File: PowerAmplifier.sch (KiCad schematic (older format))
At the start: 36 parts, among them K1 INPUT, K3 OUTPUT, P1 POWER

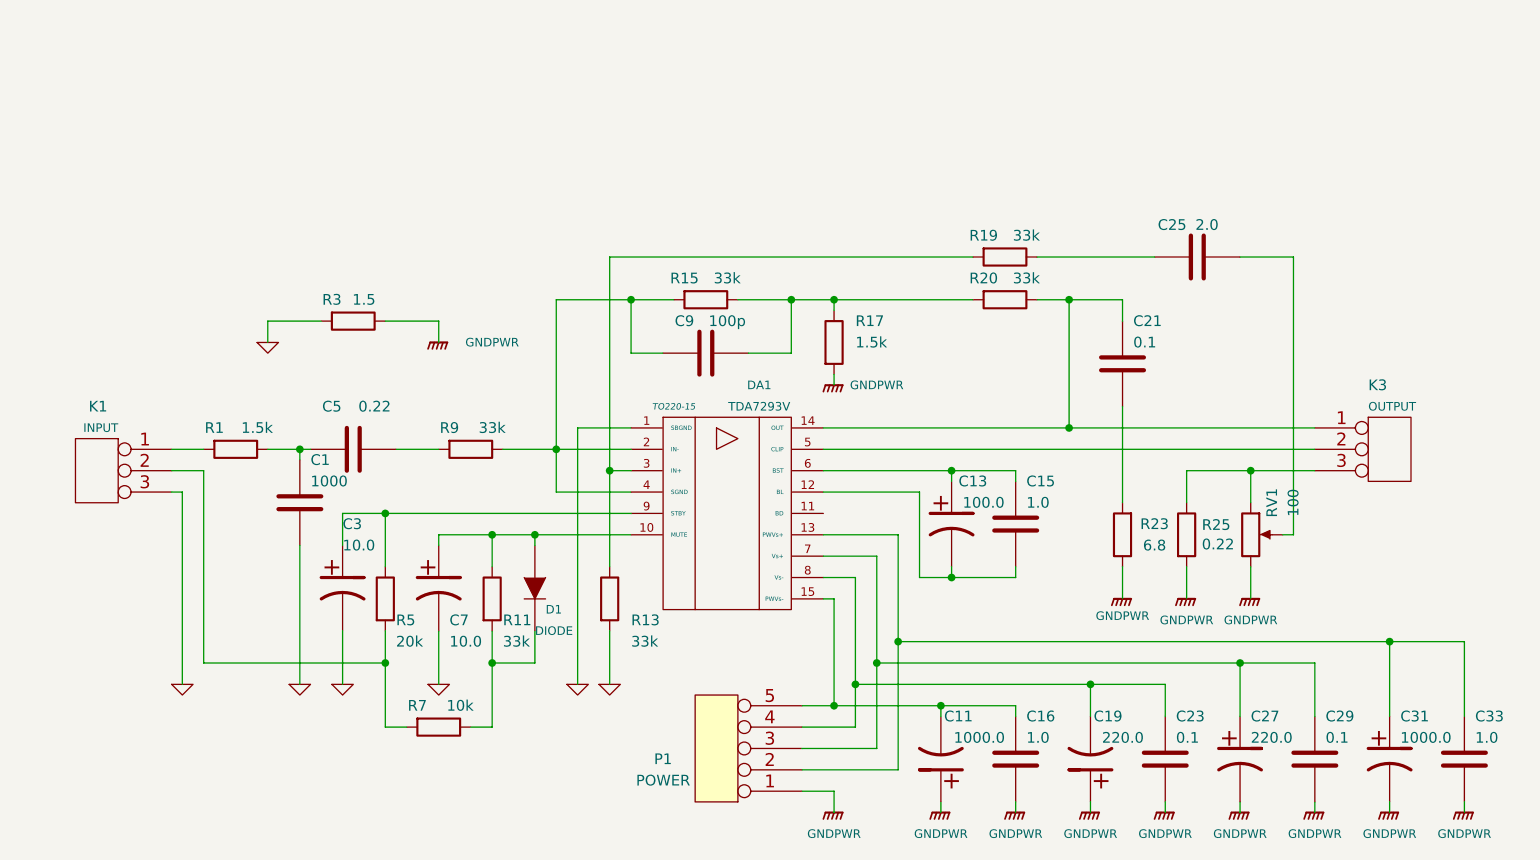
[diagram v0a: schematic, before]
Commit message: Add power to DAC
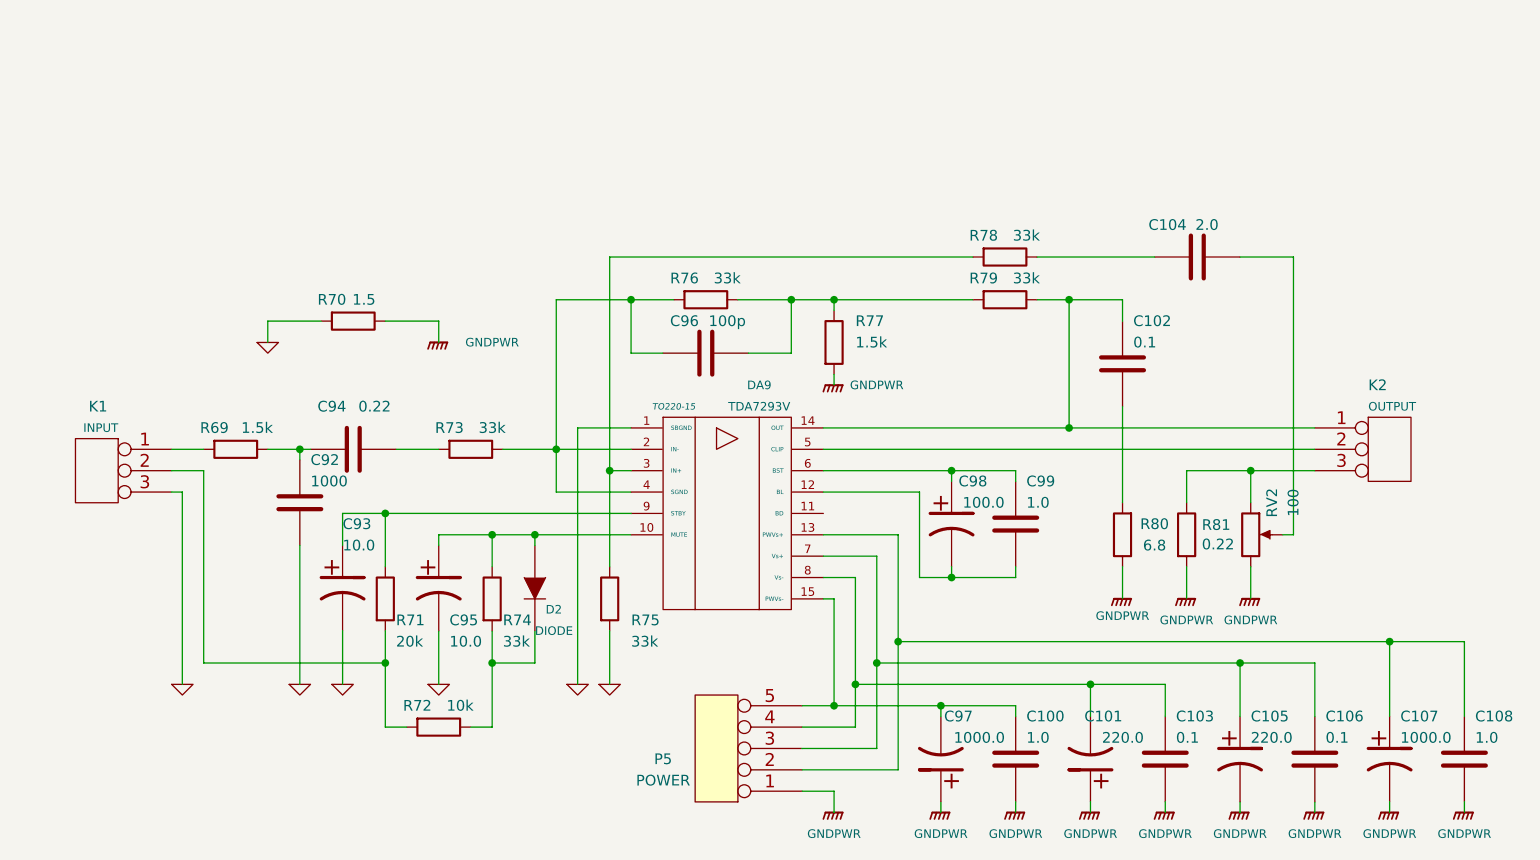
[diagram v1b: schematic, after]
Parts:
- renumbered C10 to C100, C19 to C101, C11 to C102, C13 to C103, C6 to C104, C27 to C105, C15 to C106, C31 to C107, C17 to C108, C1 to C92, C3 to C93, C3 to C94, C7 to C95, C5 to C96, C11 to C97, C13 to C98, C9 to C99, D1 to D2, DA1 to DA9, K3 to K2, P1 to P5, R1 to R69, R3 to R70, R5 to R71, R7 to R72, R9 to R73, R11 to R74, R13 to R75, R15 to R76, R17 to R77, R19 to R78, R20 to R79, R23 to R80, R25 to R81, RV1 to RV2

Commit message: Update power amplifier circuit
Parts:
- removed C104: 2.0, symbol amplifier-rescue:C-RESCUE-amplifier
- removed K2: OUTPUT, symbol amplifier-rescue:CONN_3
- added C? (x2): 82n, symbol amplifier-rescue:C-RESCUE-amplifier
- added J?: OUT, symbol amplifier-rescue:CONN_01X02
- added J?: CLIP DETECTION, symbol amplifier-rescue:CONN_01X02
- C92: value 1000 -> 750
- C94: value 0.22 -> 82n
- R73, R76, R78, R79: value 33k -> 100k
- R75: value 33k -> 200k
- R77: value 1.5k -> 3.6k
- R81: value 0.22 -> 0.15
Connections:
- net GNDPWR: now also C?.2, J?.2 (P2)
- net at C102.1, DA9.14 (OUT), R79.1: now also J?.1 (P1)
- net at DA9.3 (IN+), R75.1: now also C?.2; no longer R78.2
- net at DA9.5 (CLIP): now also J?.1 (P1)
- net at R81.1, RV2.1: now also J?.2 (P2)
- net at RV2.2: now also R78.1
- new net: C?.1, C?.1, R78.2
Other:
- moved on the sheet: C102, C96, R76, R77, R78, R79

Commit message: Update power amplifier
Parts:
- added R?: 2, symbol Device:R
- C94: value 82n -> 0.33
- R73: value 100k -> 33k; footprint (none) -> v
- R75: value 200k -> 180k
- R76, R79: value 100k -> 33k
- R77: value 3.6k -> 1.1k
- R78: value 100k -> 91k
- RV2: value 100 -> 200
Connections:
- net at J?.2 (P2), R81.1, RV2.1: now also R?.1
- net at R78.1, RV2.2: now also R?.2
- no-connect marks 0 -> 1
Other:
- moved on the sheet: C94
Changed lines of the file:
@@
 P 6400 2050
 F 0 "R79" V 6300 1950 50  0000 C CNN
-F 1 "100k" V 6300 2150 50  0000 C CNN
+F 1 "33k" V 6300 2150 50  0000 C CNN
 F 2 "" H 6400 2050 60  0001 C CNN
 F 3 "" H 6400 2050 60  0001 C CNN
@@
 P 7550 3250
 F 0 "RV2" V 7650 3400 50  0000 C CNN
-F 1 "100" V 7750 3400 50  0000 C CNN
+F 1 "200" V 7750 3400 50  0000 C CNN
 F 2 "" H 7550 3250 60  0001 C CNN
 F 3 "" H 7550 3250 60  0001 C CNN
@@
 P 5000 2050
 F 0 "R76" V 4900 1950 50  0000 C CNN
-F 1 "100k" V 4900 2150 50  0000 C CNN
+F 1 "33k" V 4900 2150 50  0000 C CNN
 F 2 "" H 5000 2050 60  0001 C CNN
 F 3 "" H 5000 2050 60  0001 C CNN
@@
 P 3900 2850
 F 0 "R73" V 3800 2750 50  0000 C CNN
-F 1 "100k" V 3800 2950 50  0000 C CNN
-F 2 "" H 3900 2850 60  0001 C CNN
+F 1 "33k" V 3800 2950 50  0000 C CNN
+F 2 "v" H 3900 2850 60  0001 C CNN
 F 3 "" H 3900 2850 60  0001 C CNN
 	1    3900 2850
@@
 P 5600 2300
 F 0 "R77" H 5700 2400 50  0000 L CNN
-F 1 "3.6k" H 5700 2300 50  0000 L CNN
+F 1 "1.1k" H 5700 2300 50  0000 L CNN
 F 2 "" H 5600 2300 60  0001 C CNN
 F 3 "" H 5600 2300 60  0001 C CNN
@@
 	4300 2850 4650 2850
 Wire Wire Line
-	3550 2850 3750 2850
+	3650 2850 3750 2850
 Connection ~ 4300 2850
 Wire Wire Line
@@
 	2950 2850 3100 2850
 Wire Wire Line
-	3100 2850 3150 2850
+	3100 2850 3250 2850
 Wire Wire Line
 	3100 2900 3100 2850
@@
 L amplifier-rescue:C-RESCUE-amplifier C?
 U 1 1 58342B6B
-P 3350 2850
+P 3450 2850
 AR Path="/58342B6B" Ref="C?"  Part="1"
 AR Path="/5833169E/58342B6B" Ref="C94"  Part="1"
-F 0 "C94" V 3150 2750 50  0000 C CNN
-F 1 "82n" V 3150 2950 50  0000 C CNN
-F 2 "" H 3350 2850 60  0001 C CNN
-F 3 "" H 3350 2850 60  0001 C CNN
-	1    3350 2850
+F 0 "C94" V 3250 2750 50  0000 C CNN
+F 1 "0.33" V 3250 2950 50  0000 C CNN
+F 2 "" H 3450 2850 60  0001 C CNN
+F 3 "" H 3450 2850 60  0001 C CNN
+	1    3450 2850
 	0    1    1    0
 $EndComp
@@
 P 4550 3550
 F 0 "R75" H 4650 3450 50  0000 L CNN
-F 1 "200k" H 4650 3350 50  0000 L CNN
+F 1 "180k" H 4650 3350 50  0000 L CNN
 F 2 "" H 4550 3550 60  0001 C CNN
 F 3 "" H 4550 3550 60  0001 C CNN
@@
 P 6400 1850
 F 0 "R78" V 6300 1750 50  0000 C CNN
-F 1 "100k" V 6300 1950 50  0000 C CNN
+F 1 "91k" V 6300 1950 50  0000 C CNN
 F 2 "" H 6400 1850 60  0001 C CNN
 F 3 "" H 6400 1850 60  0001 C CNN
@@
 	6950 3400 6950 3550
 Wire Wire Line
-	6550 1850 7750 1850
+	6550 1850 7550 1850
 $Comp
 L amplifier-rescue:C-RESCUE-amplifier C?
@@
 Wire Wire Line
 	7850 2550 7850 2650
+NoConn ~ 2700 850
+$Comp
+L Device:R R?
+U 1 1 5D817024
+P 7550 2150
+F 0 "R?" H 7480 2104 50  0000 R CNN
+F 1 "2" H 7480 2195 50  0000 R CNN
+F 2 "" V 7480 2150 50  0001 C CNN
+F 3 "~" H 7550 2150 50  0001 C CNN
+	1    7550 2150
+	-1   0    0    1
+$EndComp
+Wire Wire Line
+	7550 2300 7550 2850
+Wire Wire Line
+	7550 2000 7550 1850
+Connection ~ 7550 1850
+Wire Wire Line
+	7550 1850 7750 1850
 $EndSCHEMATC

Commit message: Modify power amplifier
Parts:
- removed R69: 1.5k, symbol amplifier-rescue:R-RESCUE-amplifier
- removed R?: 2, symbol Device:R
- C1: renamed from C94; footprint (none) -> Capacitors_ThroughHole:C_Rect_L41.5mm_W15.0mm_P37.50mm_MKS4
- C10: renamed from C106; footprint (none) -> Capacitors_ThroughHole:C_Rect_L16.5mm_W6.0mm_P15.00mm_MKT
- C101, C105: footprint (none) -> Capacitors_ThroughHole:CP_Radial_D10.0mm_P3.50mm
- C107, C97: footprint (none) -> Capacitors_ThroughHole:CP_Radial_D13.0mm_P5.00mm
- C11: renamed from C108; footprint (none) -> Capacitors_ThroughHole:C_Rect_L13.5mm_W5.0mm_P10.00mm_FKS3_FKP3_MKS4
- C2: renamed from C92; footprint (none) -> Capacitors_ThroughHole:C_Rect_L13.5mm_W5.0mm_P10.00mm_FKS3_FKP3_MKS4
- C3: renamed from C96; value 100p -> 150p; footprint (none) -> Capacitors_ThroughHole:C_Rect_L10.0mm_W4.0mm_P7.50mm_MKS4
- C4: renamed from C?; footprint (none) -> Capacitors_ThroughHole:C_Rect_L33.0mm_W13.0mm_P27.50mm_MKS4
- C5: renamed from C?; footprint (none) -> Capacitors_ThroughHole:C_Rect_L31.5mm_W13.0mm_P27.50mm_MKS4
- C6: renamed from C99; footprint (none) -> Capacitors_ThroughHole:C_Rect_L41.5mm_W15.0mm_P37.50mm_MKS4
- C7: renamed from C100; footprint (none) -> Capacitors_ThroughHole:C_Rect_L13.5mm_W5.0mm_P10.00mm_FKS3_FKP3_MKS4
- C8: renamed from C102; footprint (none) -> Capacitors_ThroughHole:C_Rect_L41.5mm_W15.0mm_P37.50mm_MKS4
- C9: renamed from C103; footprint (none) -> Capacitors_ThroughHole:C_Rect_L13.0mm_W6.0mm_P10.00mm_FKS3_FKP3_MKS4
- C93, C95, C98: footprint (none) -> Capacitors_ThroughHole:CP_Radial_D8.0mm_P3.50mm
- D2: footprint (none) -> Diodes_ThroughHole:D_DO-41_SOD81_P10.16mm_Horizontal
- DA9: footprint TO220-15 -> TO_SOT_Packages_THT:TO-220-15_Horizontal_StaggeredType1
- J13: renamed from J?; footprint (none) -> Pin_Headers:Pin_Header_Straight_1x02_Pitch2.54mm
- J14: renamed from J?; footprint (none) -> Connect:PINHEAD1-2
- K1: footprint (none) -> Pin_Headers:Pin_Header_Straight_1x02_Pitch2.54mm
- P5: footprint (none) -> Sockets_MOLEX_KK-System:Socket_MOLEX-KK-RM3-96mm_Lock_5pin_straight
- R70: footprint (none) -> Resistors_ThroughHole:R_Axial_DIN0411_L9.9mm_D3.6mm_P15.24mm_Horizontal
- R71, R72, R74, R75, R76, R77, R78, R79: footprint (none) -> Resistors_ThroughHole:R_Axial_DIN0207_L6.3mm_D2.5mm_P15.24mm_Horizontal
- R73: footprint v -> Resistors_ThroughHole:R_Axial_DIN0207_L6.3mm_D2.5mm_P15.24mm_Horizontal
- R80: footprint (none) -> Resistors_ThroughHole:R_Axial_DIN0922_L20.0mm_D9.0mm_P30.48mm_Horizontal
- R81: footprint (none) -> Resistors_ThroughHole:R_Axial_Power_L25.0mm_W9.0mm_P30.48mm
- RV2: footprint (none) -> Potentiometers:Potentiometer_Trimmer_Piher_PT-10v10_Horizontal_Px10.0mm_Py5.0mm
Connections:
- net at C3.2, DA9.2 (IN-), DA9.4 (SGND)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: now also C2.1
- net at C1.2: now also K1.1 (P1); no longer C2.1
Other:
- moved on the sheet: C92, C93, C95, D2, R71, R72, R74

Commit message: Add РЭС60 footprint
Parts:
- added C6: 750, symbol Device:C
- added K1: РЭС60, РЭС60:РЭС60, symbol рэс60:РЭС60
- added P1: Filter disable, symbol Connector:Conn_01x02_Female
- added R5: 200k, symbol Device:R_POT
- C1: renamed from C93; symbol amplifier-rescue:CP1-RESCUE-amplifier -> Device:CP
- C10: renamed from C5; value 82n -> 0.15; symbol amplifier-rescue:C-RESCUE-amplifier -> Device:C
- C11: renamed from C6; symbol amplifier-rescue:C-RESCUE-amplifier -> Device:C
- C12: renamed from C7; symbol amplifier-rescue:C-RESCUE-amplifier -> Device:C
- C13: renamed from C101; symbol amplifier-rescue:CP1-RESCUE-amplifier -> Device:CP
- C14: renamed from C8; symbol amplifier-rescue:C-RESCUE-amplifier -> Device:C
- C15: renamed from C9; symbol amplifier-rescue:C-RESCUE-amplifier -> Device:C
- C16: renamed from C105; symbol amplifier-rescue:CP1-RESCUE-amplifier -> Device:CP
- C17: renamed from C10; symbol amplifier-rescue:C-RESCUE-amplifier -> Device:C
- C18: renamed from C107; symbol amplifier-rescue:CP1-RESCUE-amplifier -> Device:CP
- C19: renamed from C11; symbol amplifier-rescue:C-RESCUE-amplifier -> Device:C
- C2: renamed from C95; symbol amplifier-rescue:CP1-RESCUE-amplifier -> Device:CP
- C3: renamed from C1; symbol amplifier-rescue:C-RESCUE-amplifier -> Device:C
- C4: renamed from C2; value 750 -> 33n; symbol amplifier-rescue:C-RESCUE-amplifier -> Device:C
- C5: renamed from C3; value 150p -> 750; symbol amplifier-rescue:C-RESCUE-amplifier -> Device:C
- C7: renamed from C4; value 82n -> 0.15; symbol amplifier-rescue:C-RESCUE-amplifier -> Device:C
- C8: renamed from C97; symbol amplifier-rescue:CP1-RESCUE-amplifier -> Device:CP
- C9: renamed from C98; symbol amplifier-rescue:CP1-RESCUE-amplifier -> Device:CP
- D1: renamed from D2; symbol amplifier-rescue:DIODE -> Device:D
- P2: renamed from K1; symbol amplifier-rescue:CONN_3 -> Connector:Conn_01x03_Female
- P3: renamed from P5; symbol amplifier-rescue:CONN_5 -> Connector:Conn_01x05_Female
- P4: renamed from J13; symbol amplifier-rescue:CONN_01X02 -> Connector:Conn_01x02_Female
- P5: renamed from J14; symbol amplifier-rescue:CONN_01X02 -> Connector:Conn_01x02_Female
- R10: renamed from R78; value 91k -> 68k
- R11: renamed from R79; value 33k -> 47k
- R4: renamed from R73; value 33k -> 47k
- R8: renamed from R76; value 33k -> 47k
- R9: renamed from R77; value 1.1k -> 1.5k
- renumbered DA9 to DA1, R71 to R1, R80 to R12, R81 to R13, R72 to R2, R74 to R3, R70 to R6, R75 to R7, RV2 to RV1
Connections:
- net GND: now also DA1.4 (SGND), K1.21; no longer C4.2
- net at C2.1, DA1.10 (MUTE), R3.1: now also D1.2 (A); no longer D1.1 (A)
- net at C14.1, DA1.14 (OUT), P5.1 (Pin_1)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: now also C6.1
- net at C4.1, R4.1, R8.2: now also R5.2, R5.3; no longer C5.2, DA1.2 (IN-), DA1.4 (SGND)
- net at R11.2, R8.1, R9.1: no longer C5.1
- net at R2.1, R3.2: now also D1.1 (K); no longer D1.2 (K)
- new net: DA1.2 (IN-), K1.12, R5.1
- new net: C4.2, K1.22
- new net: C5.1, C6.2
- new net: C5.2, K1.11
- new net: K1.B, P1.1 (Pin_1)
- new net: K1.A, P1.2 (Pin_2)
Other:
- moved on the sheet: C10, C3, C4, C5, C7, D1, R1, R10, R11, R2, R3, R4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
